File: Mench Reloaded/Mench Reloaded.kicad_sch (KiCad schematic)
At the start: 25 parts, among them IC1 DS1813, SW1 SW_Push, U1 W65C265SxQ, Y1 32.768 kHz, Y2 3.6864 mHz

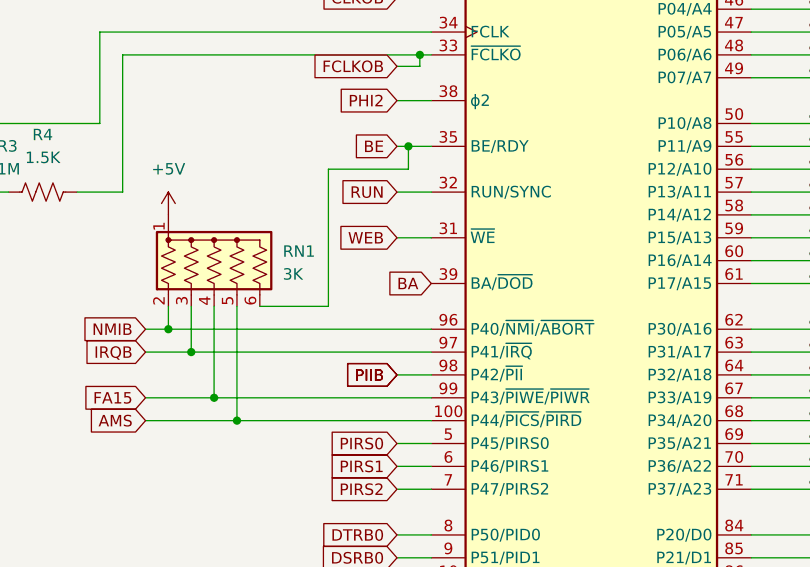
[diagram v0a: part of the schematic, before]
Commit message: Minor changes to quiet the ERC and DRC reports.
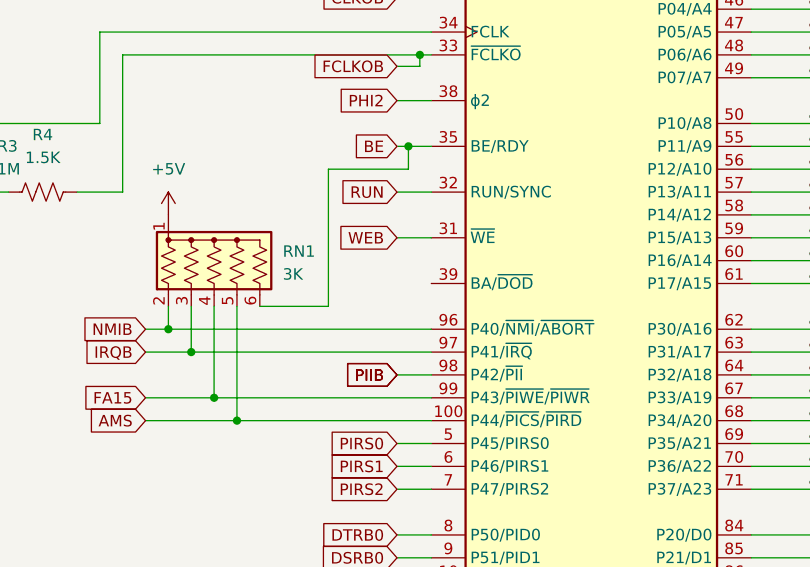
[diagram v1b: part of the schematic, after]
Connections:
- net BA: no longer names the net of U1.39 (BA/~{DOD})
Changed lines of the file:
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@@
-		)
-	)
-	(global_label "BA"
-		(shape input)
-		(at 130.81 71.12 180)
-		(fields_autoplaced yes)
-		(effects
-			(font
-				(size 1.27 1.27)
-			)
-			(justify right)
-		)
-		(property "Intersheetrefs" "${INTERSHEET_REFS}"
-			(at 125.4505 71.12 0)
-			(effects
-				(font
-					(size 1.27 1.27)
-				)
-				(justify right)
-				(hide yes)
-			)
 		)
 	)

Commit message: Added power symbols and no connect to eliminate ERC errors.
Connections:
- no-connect marks 0 -> 1
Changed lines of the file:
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@@
 		(color 0 0 0 0)
+	)
+	(no_connect
+		(at 130.81 71.12)
 	)
 	(bus_entry

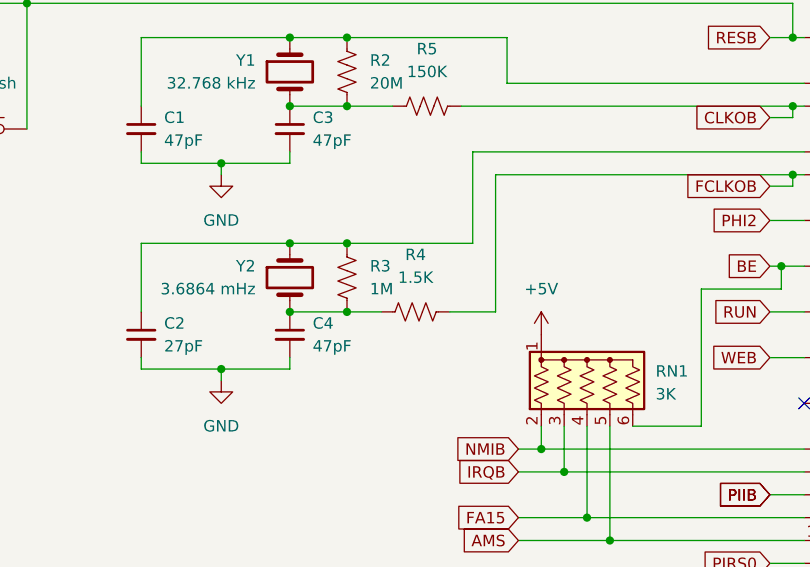
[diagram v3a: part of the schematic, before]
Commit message: Changed values for C2 and C4 to match datasheet and testing.
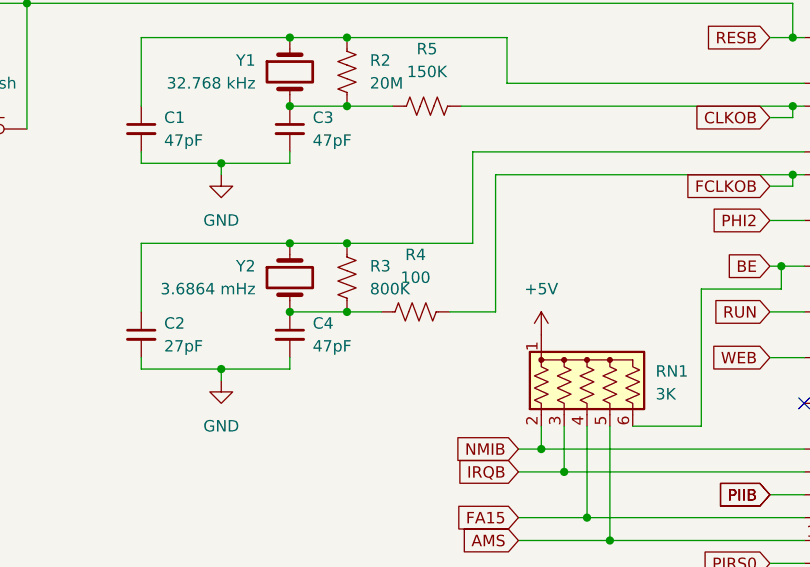
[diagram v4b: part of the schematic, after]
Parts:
- R3: value 1M -> 800K
- R4: value 1.5K -> 100
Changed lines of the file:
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@@
 			)
 		)
-		(property "Value" "1.5K"
+		(property "Value" "100"
 			(at 87.63 57.15 90)
 			(effects
@@
 			)
 		)
-		(property "Value" "1M"
+		(property "Value" "800K"
 			(at 82.55 58.42 0)
 			(effects
